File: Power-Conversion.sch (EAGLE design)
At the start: 41 parts

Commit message: prelim sch
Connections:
- removed net N$11: R2.1, U$5.C, U$7.D1
- net ONOFF: now also R2.1, U$5.C, U$7.D1
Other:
- note removed: "need optoisolator here to avoid gnd loop"
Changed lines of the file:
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@@
 <sheet>
 <plain>
-<text x="60.96" y="121.92" size="1.778" layer="91">need optoisolator here
-to avoid gnd loop</text>
 </plain>
 <instances>
@@
 <net name="ONOFF" class="0">
 <segment>
-<wire x1="104.14" y1="116.84" x2="91.44" y2="116.84" width="0.1524" layer="91"/>
 <label x="91.44" y="116.84" size="1.778" layer="95"/>
 <pinref part="U$3" gate="G$1" pin="ON/OFF"/>
+<pinref part="U$7" gate="G$1" pin="D1"/>
+<pinref part="R2" gate="G$1" pin="1"/>
+<wire x1="48.26" y1="116.84" x2="55.88" y2="116.84" width="0.1524" layer="91"/>
+<wire x1="55.88" y1="116.84" x2="63.5" y2="116.84" width="0.1524" layer="91"/>
+<pinref part="U$5" gate="G$1" pin="C"/>
+<wire x1="63.5" y1="106.68" x2="63.5" y2="116.84" width="0.1524" layer="91"/>
+<wire x1="63.5" y1="116.84" x2="104.14" y2="116.84" width="0.1524" layer="91"/>
 </segment>
 <segment>
@@
 </segment>
 </net>
-<net name="N$11" class="0">
-<segment>
-<pinref part="U$7" gate="G$1" pin="D1"/>
-<pinref part="R2" gate="G$1" pin="1"/>
-<wire x1="48.26" y1="116.84" x2="55.88" y2="116.84" width="0.1524" layer="91"/>
-<wire x1="55.88" y1="116.84" x2="63.5" y2="116.84" width="0.1524" layer="91"/>
-<pinref part="U$5" gate="G$1" pin="C"/>
-<wire x1="63.5" y1="116.84" x2="68.58" y2="116.84" width="0.1524" layer="91"/>
-<wire x1="63.5" y1="106.68" x2="63.5" y2="116.84" width="0.1524" layer="91"/>
-</segment>
-</net>
 </nets>
 </sheet>
@@
 </schematic>
 </drawing>
-<compatibility>
-<note version="6.3" minversion="6.2.2" severity="warning">
-Since Version 6.2.2 text objects can contain more than one line,
-which will not be processed correctly with this version.
-</note>
-</compatibility>
 </eagle>

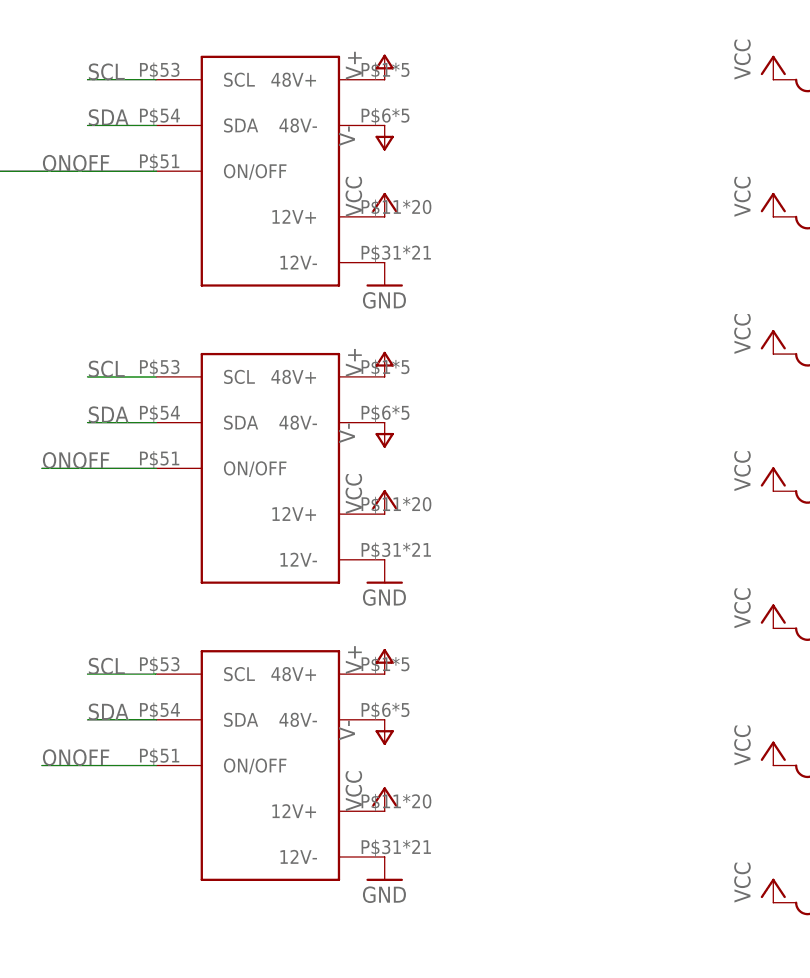
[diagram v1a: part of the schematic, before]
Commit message: 2 layer power input/output
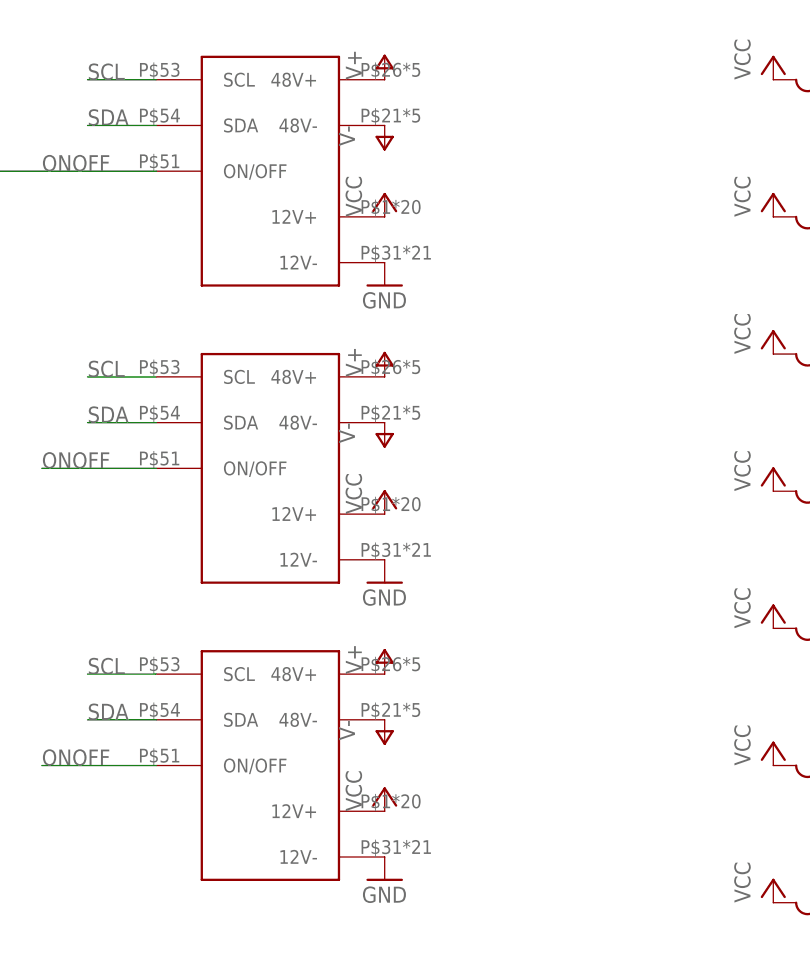
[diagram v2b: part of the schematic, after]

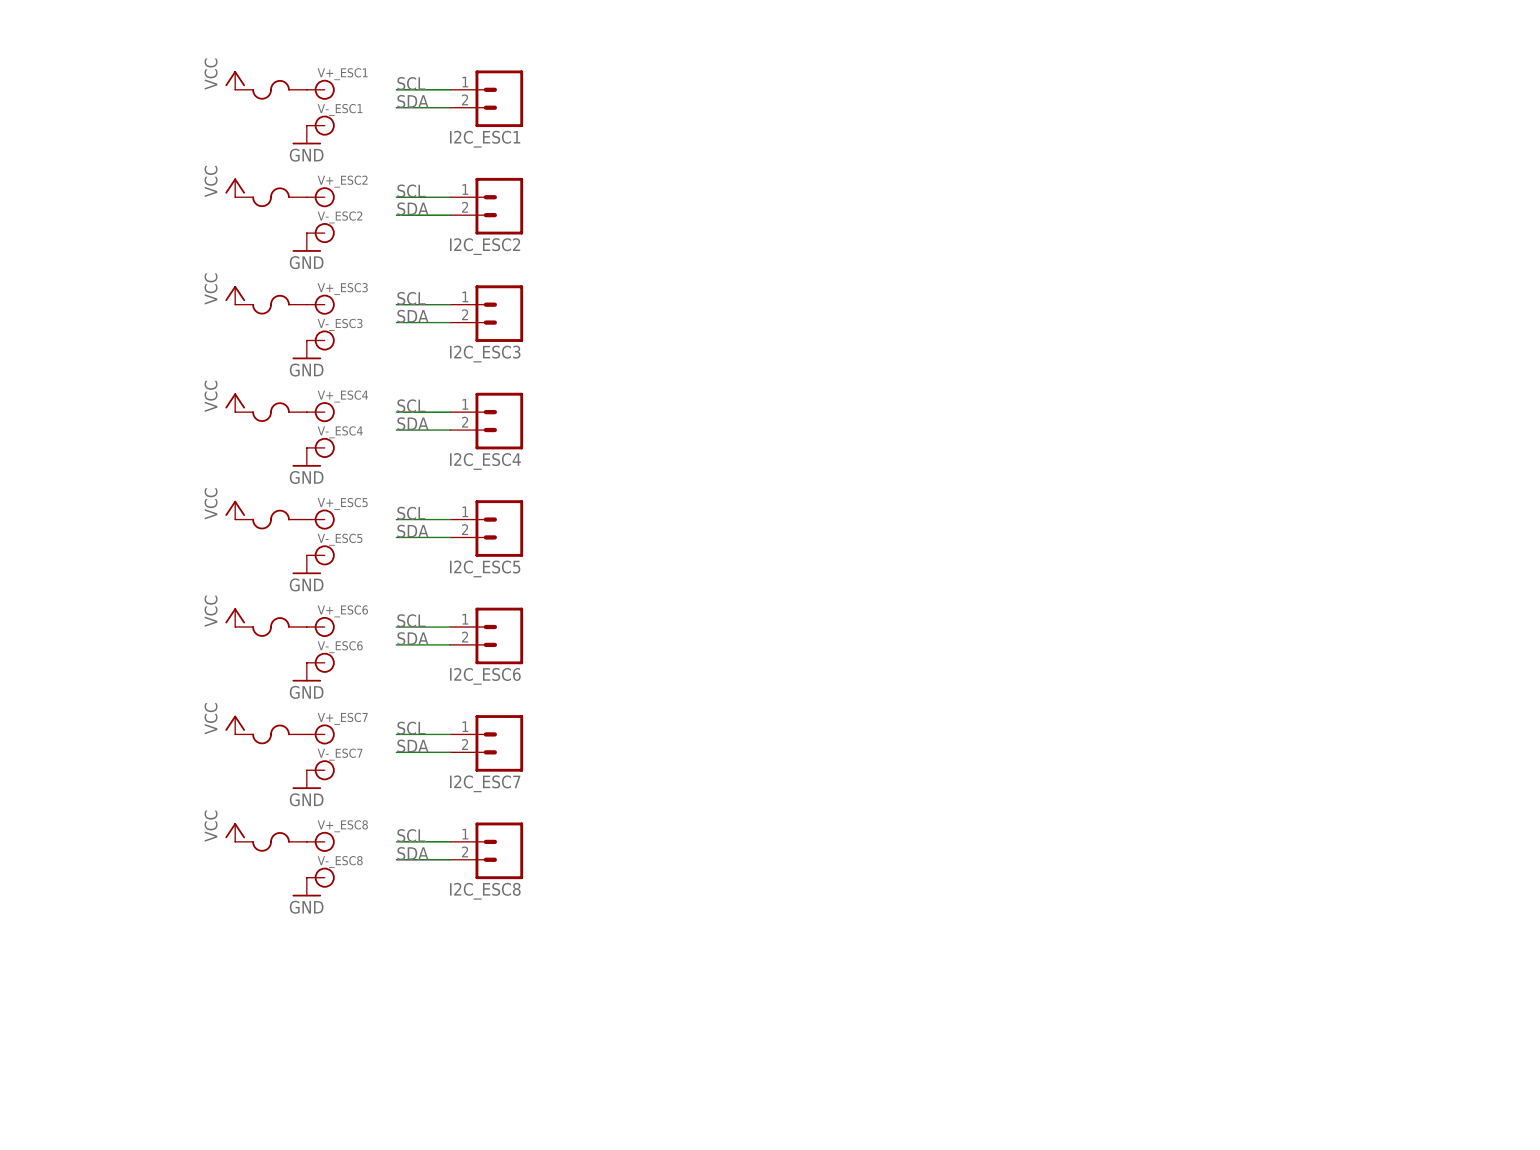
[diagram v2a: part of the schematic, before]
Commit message: Fuse and prelim MCU connections
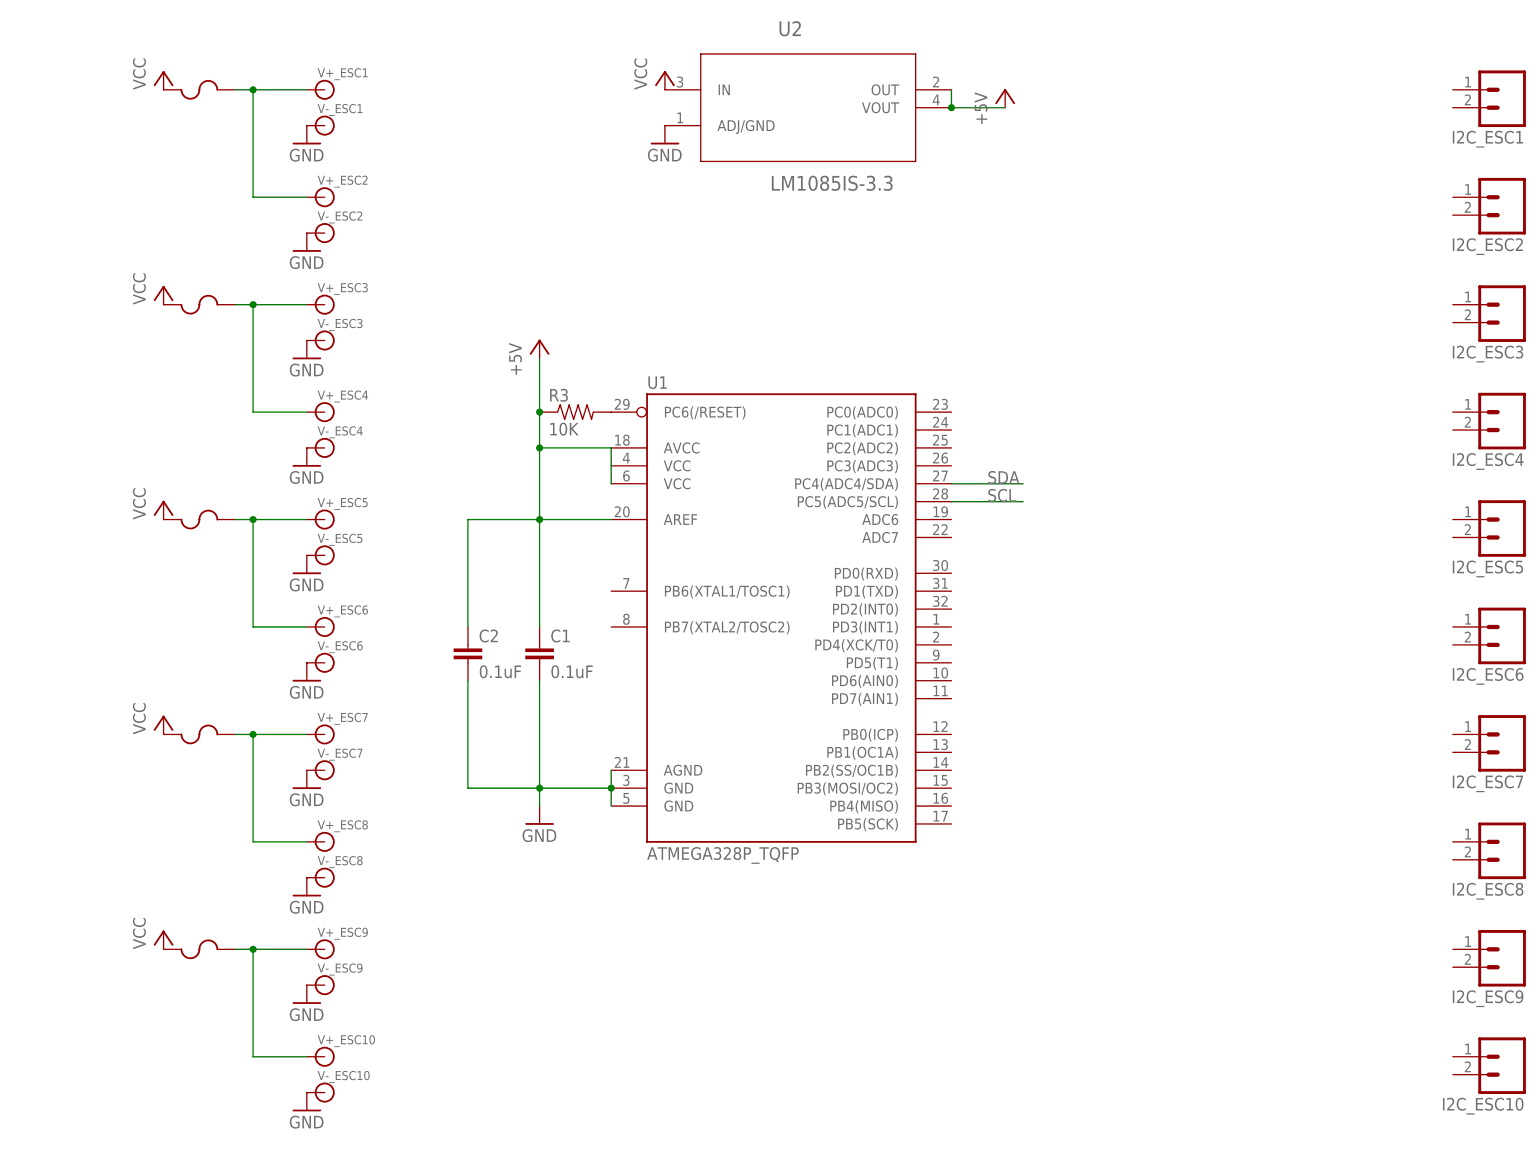
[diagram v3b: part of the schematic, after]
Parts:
- removed F4, F6, F8: (no value), MotherboardParts:KEYSTONE_FUSE_3587
- added C1, C2: 0.1uF, SparkFun-Capacitors:0.1UF-25V(+80/-20%)(0603)
- added I2C_ESC10, I2C_ESC9: (no value), SparkFun-Connectors:M02PTH
- added R3: 10K, SparkFun-Resistors:10KOHM-1/10W-1%(0603)0603
- added U1: ATMEGA328P_TQFP, SparkFun-DigitalIC:ATMEGA328P_TQFP
- added U2: LM1085IS-3.3, PowerComponents:LM1085IS-3.3
- added V+_ESC10, V+_ESC9, V-_ESC10, V-_ESC9: (no value), SparkFun-Connectors:BANANA_CONN
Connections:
- removed net N$2: F2.P$2, V+_ESC2.1
- removed net N$4: F4.P$2, V+_ESC4.1
- removed net N$6: F6.P$2, V+_ESC6.1
- removed net N$8: F8.P$2, V+_ESC8.1
- new net +5V: C1.1, C2.1, R3.1, U1.AREF, U1.AVCC, U1.VCC@4, U1.VCC@6, U2.OUT, U2.VOUT
- new net N$11: F2.P$2, V+_ESC10.1, V+_ESC9.1
- new net N$13: R3.2, U1.PC6(/RESET)
- net GND: now also C1.2, C2.2, U1.AGND, U1.GND@3, U1.GND@5, U2.ADJ/GND, V-_ESC10.1, V-_ESC9.1
- net N$1: now also V+_ESC2.1
- net N$3: now also V+_ESC4.1
- net N$5: now also V+_ESC6.1
- net N$7: now also V+_ESC8.1
- net SCL: now also U1.PC5(ADC5/SCL); no longer I2C_ESC1.1, I2C_ESC2.1, I2C_ESC3.1, I2C_ESC4.1, I2C_ESC5.1, I2C_ESC6.1, I2C_ESC7.1, I2C_ESC8.1
- net SDA: now also U1.PC4(ADC4/SDA); no longer I2C_ESC1.2, I2C_ESC2.2, I2C_ESC3.2, I2C_ESC4.2, I2C_ESC5.2, I2C_ESC6.2, I2C_ESC7.2, I2C_ESC8.2
- net VCC: now also U2.IN; no longer F4.P$1, F6.P$1, F8.P$1
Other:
- moved on the sheet: I2C_ESC1, I2C_ESC2, I2C_ESC3, I2C_ESC4, I2C_ESC5, I2C_ESC6, I2C_ESC7, I2C_ESC8

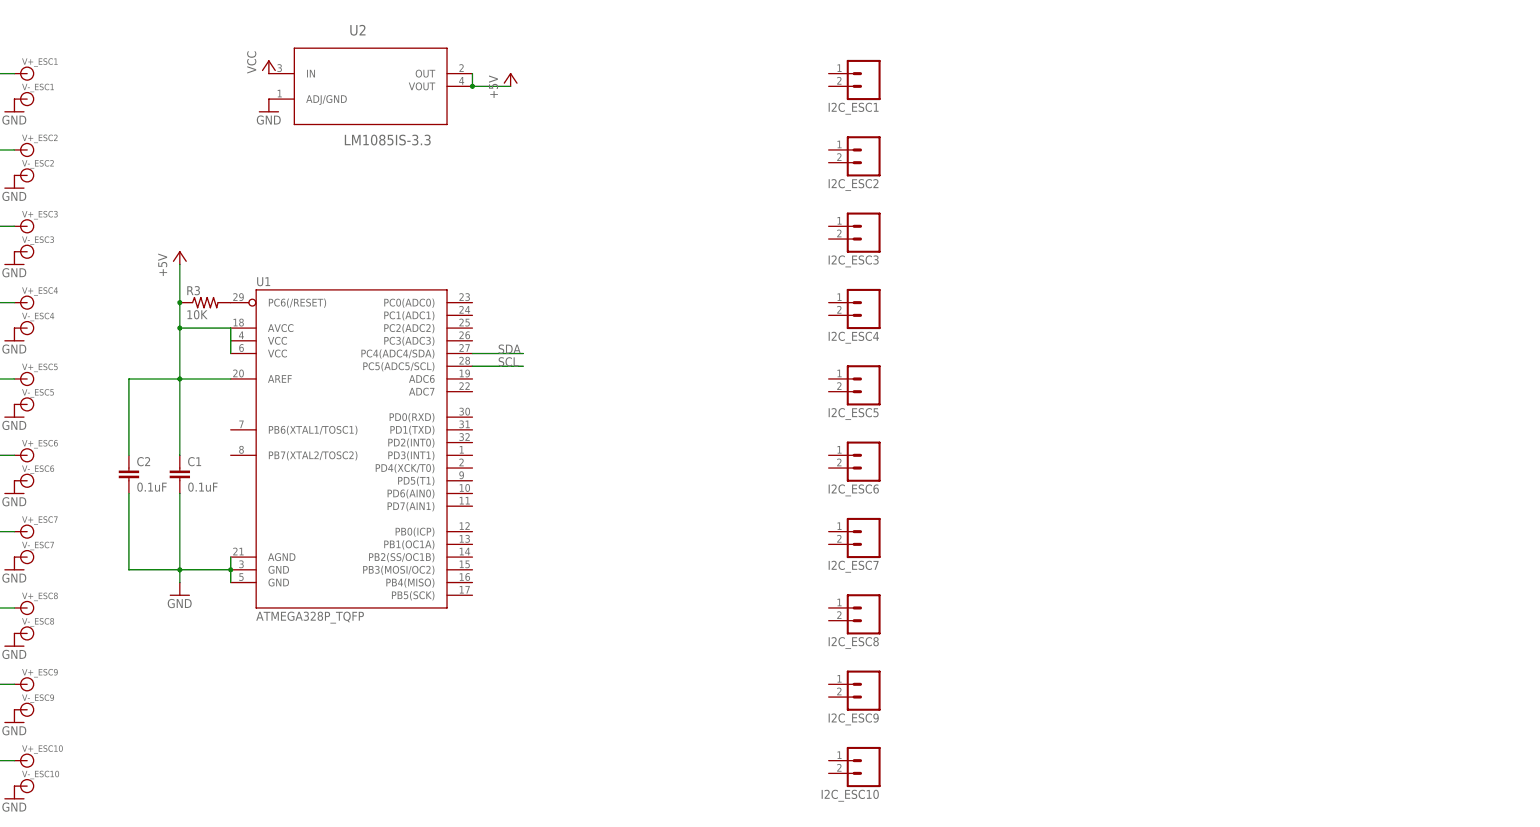
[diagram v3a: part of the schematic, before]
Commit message: Placement and early routing of AVR board
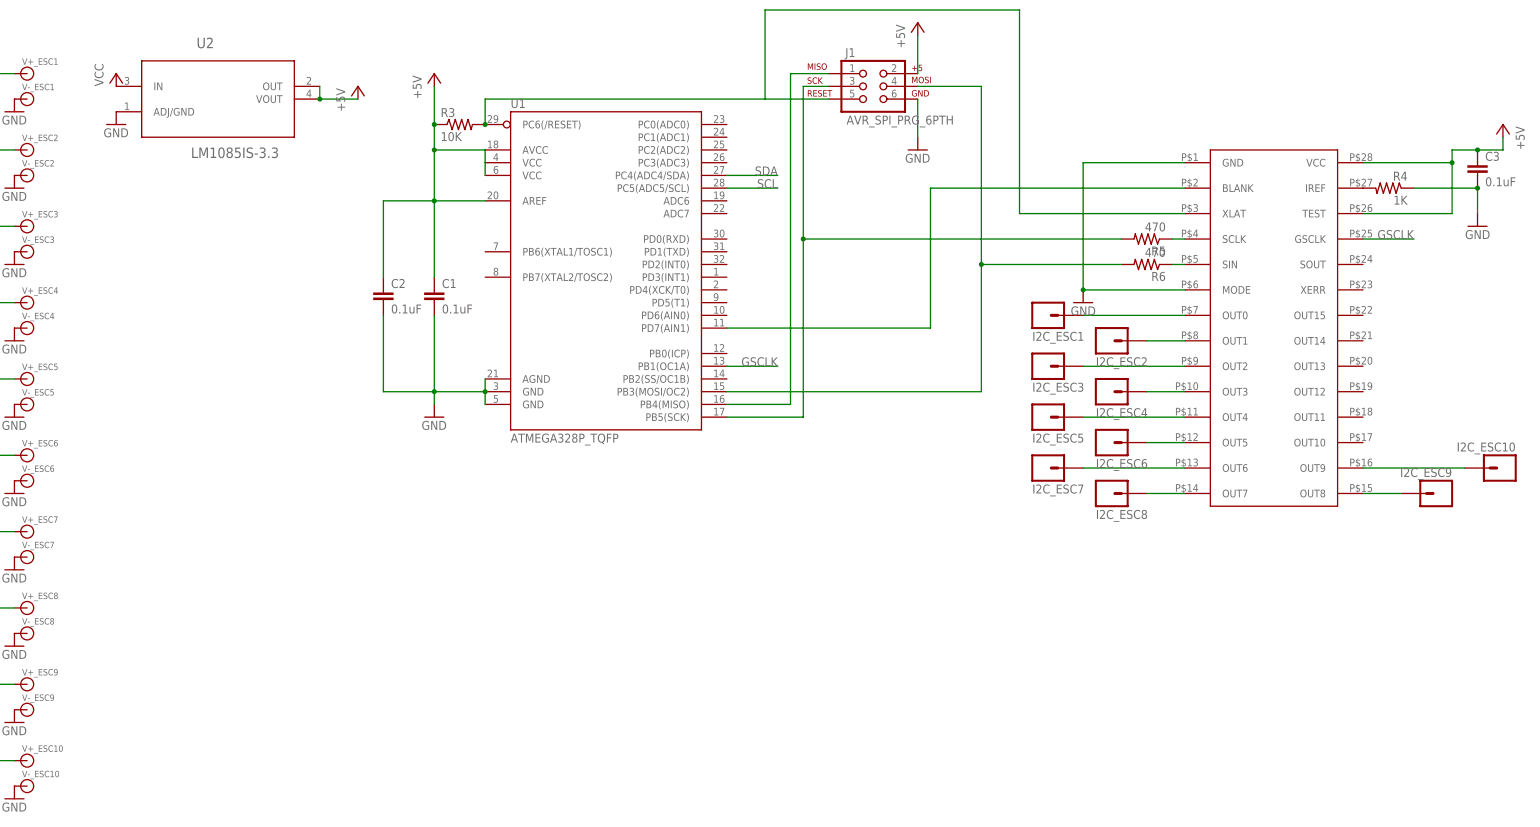
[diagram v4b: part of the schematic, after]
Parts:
- added C3: 0.1uF, SparkFun-Capacitors:0.1UF-25V(+80/-20%)(0603)
- added J1: AVR_SPI_PRG_6PTH, SparkFun-Connectors:AVR_SPI_PRG_6PTH
- added R4: 1K, SparkFun-Resistors:1KOHM-1/10W-1%(0603)
- added R5, R6: 470, SparkFun-Resistors:470OHM1/10W1%(0603)
- added U$8: TLC59401PWPR, MotherboardParts:TLC59401PWPR
- I2C_ESC1, I2C_ESC10, I2C_ESC2, I2C_ESC3, I2C_ESC4, I2C_ESC5, I2C_ESC6, I2C_ESC7, I2C_ESC8, I2C_ESC9: device SparkFun-Connectors:M02PTH -> SparkFun-Connectors:M01PTH
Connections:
- new net GSCLK: U$8.GSCLK, U1.PB1(OC1A)
- new net N$12: R5.1, U$8.SCLK
- new net N$14: R6.1, U$8.SIN
- new net N$15: I2C_ESC1.1, U$8.OUT0
- new net N$16: I2C_ESC2.1, U$8.OUT1
- new net N$17: I2C_ESC3.1, U$8.OUT2
- new net N$18: I2C_ESC4.1, U$8.OUT3
- new net N$19: I2C_ESC5.1, U$8.OUT4
- new net N$20: I2C_ESC6.1, U$8.OUT5
- new net N$21: I2C_ESC7.1, U$8.OUT6
- new net N$22: I2C_ESC8.1, U$8.OUT7
- new net N$23: I2C_ESC9.1, U$8.OUT8
- new net N$24: I2C_ESC10.1, U$8.OUT9
- new net N$25: R4.2, U$8.IREF
- new net N$26: J1.4, R6.2, U1.PB3(MOSI/OC2)
- new net N$27: U$8.BLANK, U1.PD7(AIN1)
- new net N$29: J1.1, U1.PB4(MISO)
- new net N$31: J1.3, R5.2, U1.PB5(SCK)
- net +5V: now also C3.1, J1.2, U$8.TEST, U$8.VCC
- net GND: now also C3.2, J1.6, R4.1, U$8.GND, U$8.MODE
- net N$13: now also J1.5, U$8.XLAT
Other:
- moved on the sheet: C1, C2, R3, U1, U2
